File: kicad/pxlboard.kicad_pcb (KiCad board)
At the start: 2 copper layers, 72.6 x 78.2 mm, 68 parts, among them U2 LIS3DHTR

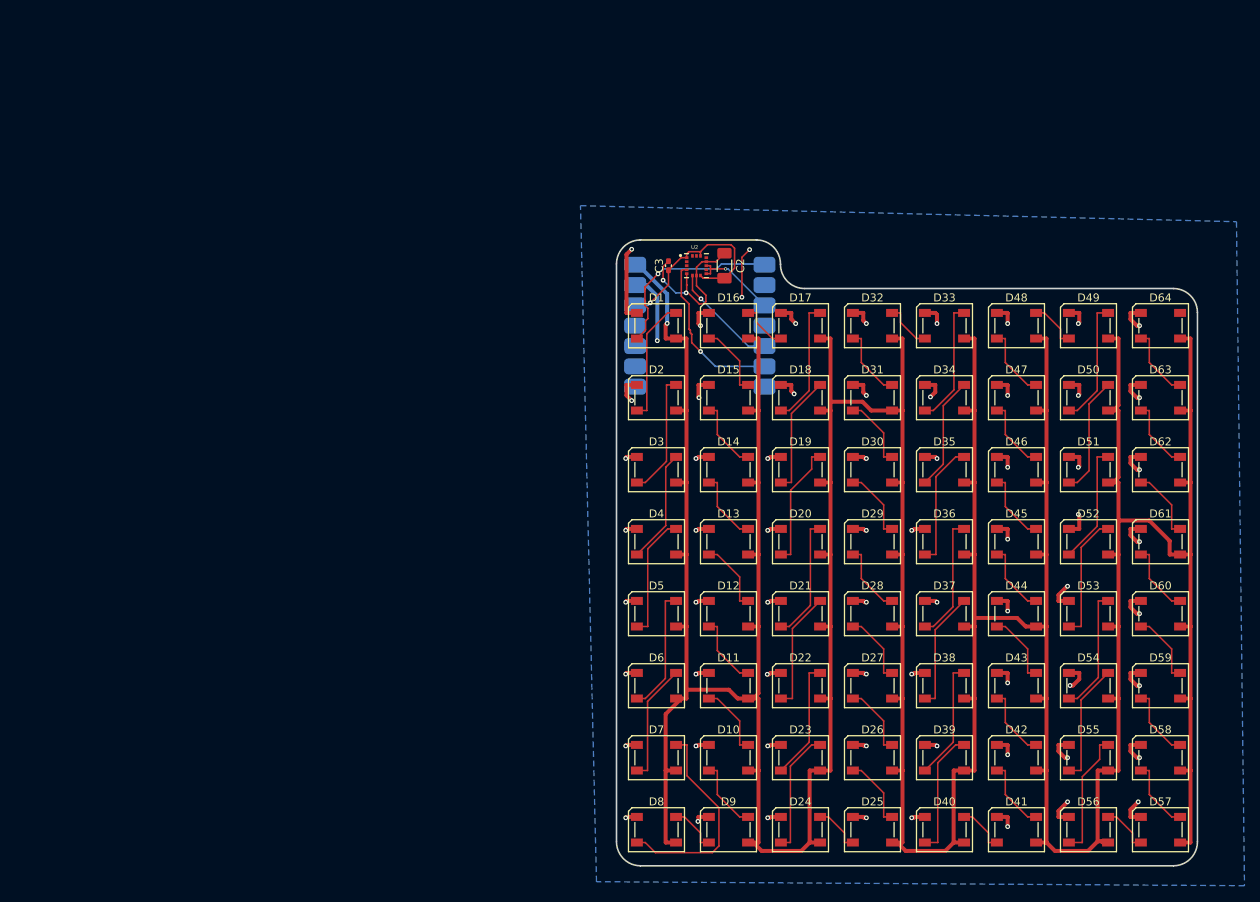
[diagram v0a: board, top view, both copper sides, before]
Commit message: feat: add caps and reroute
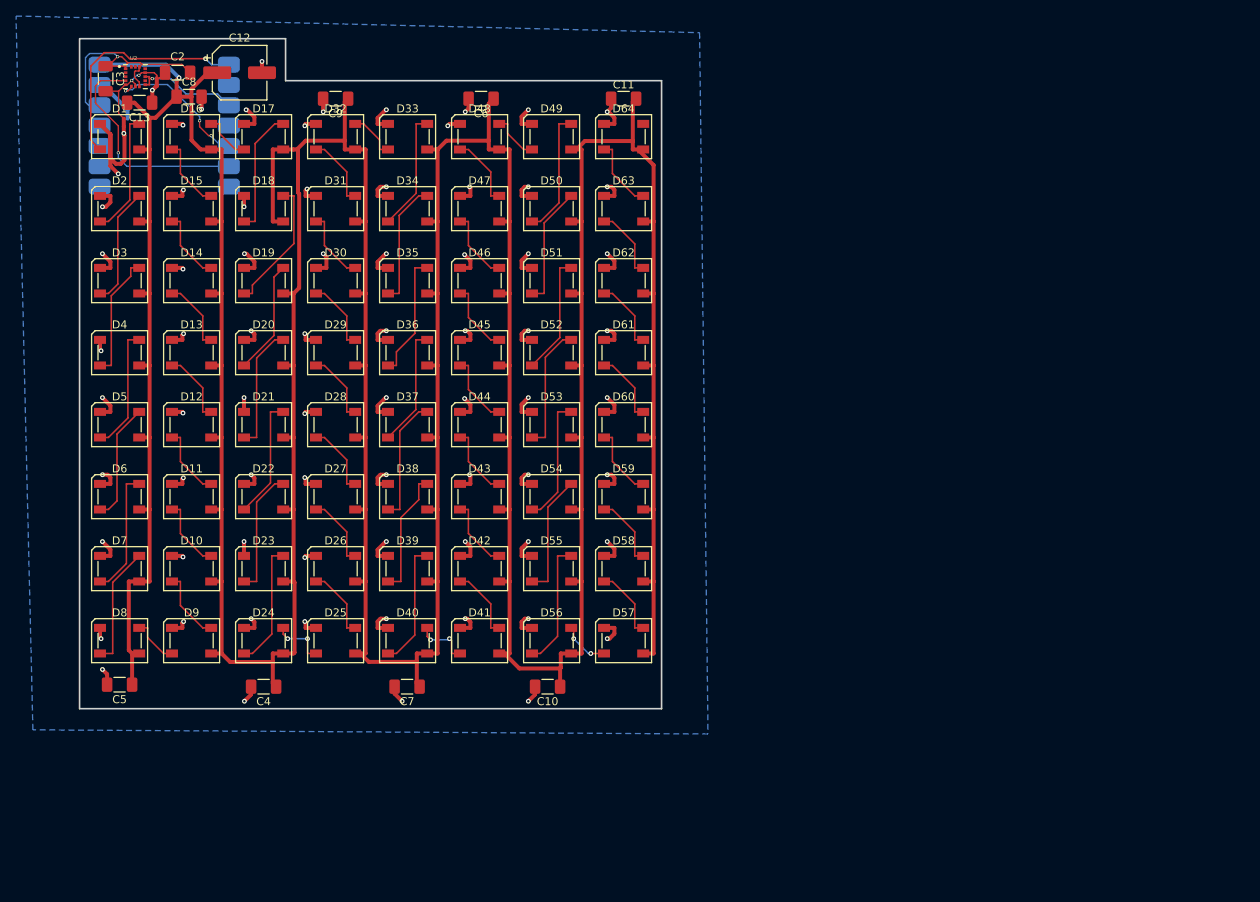
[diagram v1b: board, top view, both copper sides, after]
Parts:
- added C10: 10uf, Capacitor_SMD:C_1206_3216Metric_Pad1.33x1.80mm_HandSolder, F.Cu at (107.4, 102.1)
- added C11: 10uf, Capacitor_SMD:C_1206_3216Metric_Pad1.33x1.80mm_HandSolder, F.Cu at (116.9, 28.6)
- added C12: 470uf, Capacitor_SMD:CP_Elec_6.3x9.9, F.Cu at (68.9, 25.4)
- added C13: 100nf, Capacitor_SMD:C_1206_3216Metric_Pad1.33x1.80mm_HandSolder, F.Cu at (56.4, 29.1)
- added C4: 10uf, Capacitor_SMD:C_1206_3216Metric_Pad1.33x1.80mm_HandSolder, F.Cu at (71.9, 102.1)
- added C5: 10uf, Capacitor_SMD:C_1206_3216Metric_Pad1.33x1.80mm_HandSolder, F.Cu at (53.9, 101.9)
- added C6: 10uf, Capacitor_SMD:C_1206_3216Metric_Pad1.33x1.80mm_HandSolder, F.Cu at (99.1, 28.6)
- added C7: 10uf, Capacitor_SMD:C_1206_3216Metric_Pad1.33x1.80mm_HandSolder, F.Cu at (89.8, 102.1)
- added C8: 10uf, Capacitor_SMD:C_1206_3216Metric_Pad1.33x1.80mm_HandSolder, F.Cu at (62.6, 28.4)
- added C9: 10uf, Capacitor_SMD:C_1206_3216Metric_Pad1.33x1.80mm_HandSolder, F.Cu at (80.9, 28.6)
- added NT1: NetTie_2, NetTie:NetTie-2_SMD_Pad0.5mm, F.Cu at (54.4, 31.6)
- added NT2: NetTie_2, NetTie:NetTie-2_SMD_Pad0.5mm, F.Cu at (58.5, 26.6)
- C3: value 10uf -> 10nf; footprint Capacitor_SMD:C_0402_1005Metric_Pad0.74x0.62mm_HandSolder -> Capacitor_SMD:C_1206_3216Metric_Pad1.33x1.80mm_HandSolder
- moved C3 74.1 mm to (52.1, 26.1), turned to -90 degrees
- moved U2 74.0 mm to (55.9, 25.9)
- moved C2 72.5 mm to (61.1, 25.4), turned to 180 degrees
- moved XIAO RP2040 71.5 mm to (59.6, 32.0)
- moved D1 71.2 mm to (53.9, 33.4)
- moved D10 71.2 mm to (62.9, 87.4)
- moved D11 71.2 mm to (62.9, 78.4)
- moved D12 71.2 mm to (62.9, 69.4)
- moved D13 71.2 mm to (62.9, 60.4)
- moved D14 71.2 mm to (62.9, 51.4)
- moved D15 71.2 mm to (62.9, 42.4)
- moved D16 71.2 mm to (62.9, 33.4)
- moved D17 71.2 mm to (71.9, 33.4)
- moved D18 71.2 mm to (71.9, 42.4)
- moved D19 71.2 mm to (71.9, 51.4)
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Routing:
- net +5V: track 663.3 -> 726.5 mm
- net GND: track 175.9 -> 214.7 mm, vias 67 -> 74
- net Net-(D7-DOUT): track 26.8 -> 15.2 mm
- net SCL: track 21.0 -> 28.5 mm
- net GND tiny: track 20.8 -> 13.8 mm
- net NEOPIXEL_SIG: track 23.3 -> 29.5 mm
- net +3.3V: track 25.0 -> 30.8 mm
- net SDA: track 13.7 -> 18.2 mm, vias 1 -> 3
- net INT1: track 10.7 -> 13.4 mm
- net Net-(D18-DOUT): track 15.0 -> 16.7 mm
- net Net-(D3-DOUT): track 14.2 -> 15.7 mm
- net Net-(D34-DOUT): track 14.2 -> 15.7 mm
- net Net-(D19-DOUT): track 15.6 -> 14.2 mm
- net NEOPIXEL_SIG_ROW5: track 6.13 -> 7.10 mm, vias 0 -> 2
- net NEOPIXEL_SIG_ROW3: track 6.13 -> 6.96 mm, vias 0 -> 2
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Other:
- board size 72.6 x 78.2 mm -> 72.8 x 83.8 mm
